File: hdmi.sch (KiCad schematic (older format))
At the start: 31 parts, among them J1901 Mini-HDMI, Q1901 NX3020NAKS, Q1902 NX3020NAKS, Q1903 NX3020NAKS, Q1904 NX3020NAKS, U1901 PCMF3HDMI2SZ, U1902 PCMF2HDMI2SZ

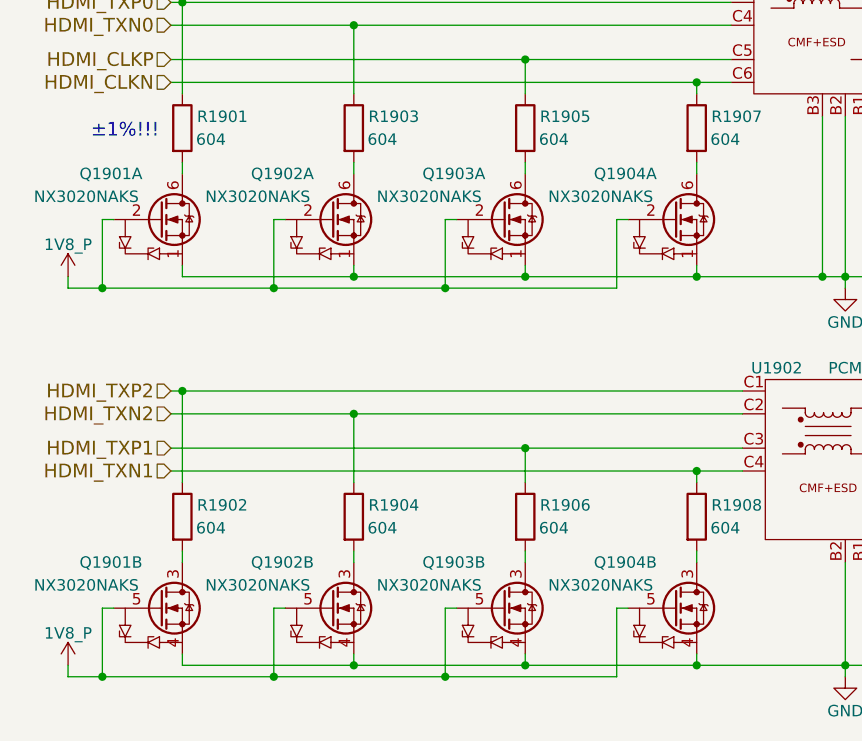
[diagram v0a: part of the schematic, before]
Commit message: Add preliminary Bill-of-Materials, fill in more missing component information such as inductor selection for the 3V3(_P) rail
Most critical components should now be getting ordered.
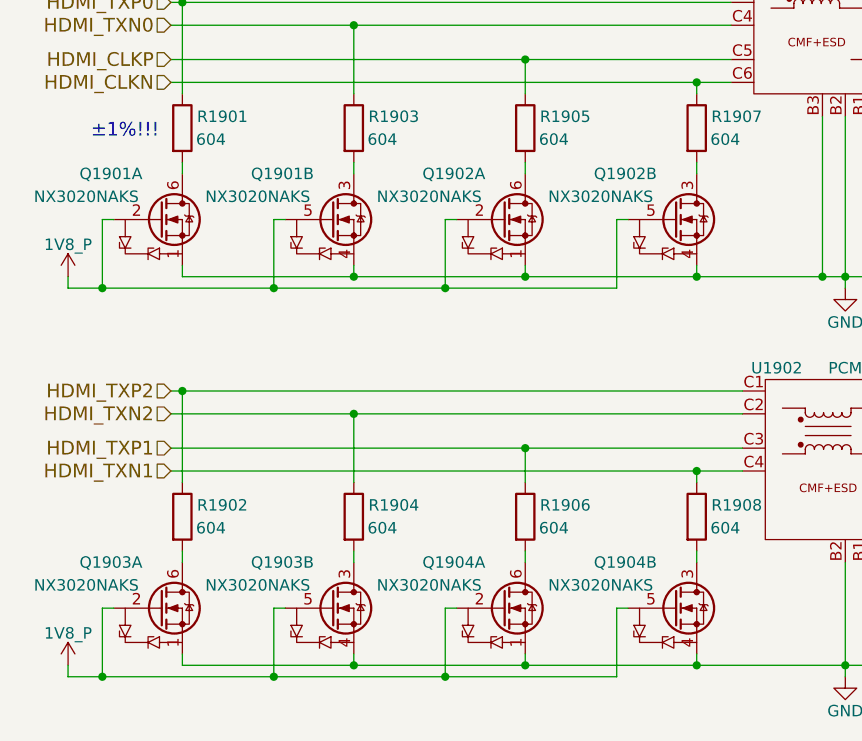
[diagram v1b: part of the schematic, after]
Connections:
- net at Q1902.6 (D): now also R1905.2; no longer R1903.2
- net at Q1903.6 (D): now also R1902.2; no longer R1905.2
- net at Q1904.6 (D): now also R1906.2; no longer R1907.2
- net at Q1901.3 (D): now also R1903.2; no longer R1902.2
- net at Q1902.3 (D): now also R1907.2; no longer R1904.2
- net at Q1903.3 (D): now also R1904.2; no longer R1906.2
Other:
- moved on the sheet: Q1901B, Q1902A, Q1902B, Q1903A, Q1903B, Q1904A
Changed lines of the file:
@@
 L Q_NMOS_DUAL Q1902
 U 1 1 5B013E98
-P 1800 3100
-F 0 "Q1902" H 1450 3300 50  0000 L CNN
-F 1 "NX3020NAKS" H 1250 3200 50  0000 L CNN
-F 2 "" H 2000 3200 50  0001 C CNN
-F 3 "" H 1800 3100 50  0001 C CNN
-	1    1800 3100
+P 2550 3100
+F 0 "Q1902" H 2200 3300 50  0000 L CNN
+F 1 "NX3020NAKS" H 2000 3200 50  0000 L CNN
+F 2 "" H 2750 3200 50  0001 C CNN
+F 3 "" H 2550 3100 50  0001 C CNN
+	1    2550 3100
 	1    0    0    -1
 $EndComp
@@
 L Q_NMOS_DUAL Q1903
 U 1 1 5B014489
-P 2550 3100
-F 0 "Q1903" H 2200 3300 50  0000 L CNN
-F 1 "NX3020NAKS" H 2000 3200 50  0000 L CNN
-F 2 "" H 2750 3200 50  0001 C CNN
-F 3 "" H 2550 3100 50  0001 C CNN
-	1    2550 3100
+P 1050 4800
+F 0 "Q1903" H 700 5000 50  0000 L CNN
+F 1 "NX3020NAKS" H 500 4900 50  0000 L CNN
+F 2 "" H 1250 4900 50  0001 C CNN
+F 3 "" H 1050 4800 50  0001 C CNN
+	1    1050 4800
 	1    0    0    -1
 $EndComp
@@
 L Q_NMOS_DUAL Q1904
 U 1 1 5B014490
-P 3300 3100
-F 0 "Q1904" H 2950 3300 50  0000 L CNN
-F 1 "NX3020NAKS" H 2750 3200 50  0000 L CNN
-F 2 "" H 3500 3200 50  0001 C CNN
-F 3 "" H 3300 3100 50  0001 C CNN
-	1    3300 3100
+P 2550 4800
+F 0 "Q1904" H 2200 5000 50  0000 L CNN
+F 1 "NX3020NAKS" H 2000 4900 50  0000 L CNN
+F 2 "" H 2750 4900 50  0001 C CNN
+F 3 "" H 2550 4800 50  0001 C CNN
+	1    2550 4800
 	1    0    0    -1
 $EndComp
@@
 L Q_NMOS_DUAL Q1901
 U 2 1 5B019D36
-P 1050 4800
-F 0 "Q1901" H 700 5000 50  0000 L CNN
-F 1 "NX3020NAKS" H 500 4900 50  0000 L CNN
-F 2 "" H 1250 4900 50  0001 C CNN
-F 3 "" H 1050 4800 50  0001 C CNN
-	2    1050 4800
+P 1800 3100
+F 0 "Q1901" H 1450 3300 50  0000 L CNN
+F 1 "NX3020NAKS" H 1250 3200 50  0000 L CNN
+F 2 "" H 2000 3200 50  0001 C CNN
+F 3 "" H 1800 3100 50  0001 C CNN
+	2    1800 3100
 	1    0    0    -1
 $EndComp
@@
 L Q_NMOS_DUAL Q1902
 U 2 1 5B019D3C
-P 1800 4800
-F 0 "Q1902" H 1450 5000 50  0000 L CNN
-F 1 "NX3020NAKS" H 1250 4900 50  0000 L CNN
-F 2 "" H 2000 4900 50  0001 C CNN
-F 3 "" H 1800 4800 50  0001 C CNN
-	2    1800 4800
+P 3300 3100
+F 0 "Q1902" H 2950 3300 50  0000 L CNN
+F 1 "NX3020NAKS" H 2750 3200 50  0000 L CNN
+F 2 "" H 3500 3200 50  0001 C CNN
+F 3 "" H 3300 3100 50  0001 C CNN
+	2    3300 3100
 	1    0    0    -1
 $EndComp
@@
 L Q_NMOS_DUAL Q1903
 U 2 1 5B019D4E
-P 2550 4800
-F 0 "Q1903" H 2200 5000 50  0000 L CNN
-F 1 "NX3020NAKS" H 2000 4900 50  0000 L CNN
-F 2 "" H 2750 4900 50  0001 C CNN
-F 3 "" H 2550 4800 50  0001 C CNN
-	2    2550 4800
+P 1800 4800
+F 0 "Q1903" H 1450 5000 50  0000 L CNN
+F 1 "NX3020NAKS" H 1250 4900 50  0000 L CNN
+F 2 "" H 2000 4900 50  0001 C CNN
+F 3 "" H 1800 4800 50  0001 C CNN
+	2    1800 4800
 	1    0    0    -1
 $EndComp

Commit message: Add decoupling/stitching capacitors to the 5V_P, 3V3_P, and 1V8_P rails which will be spread through the respective power planes (not necessarily having to be near chips)
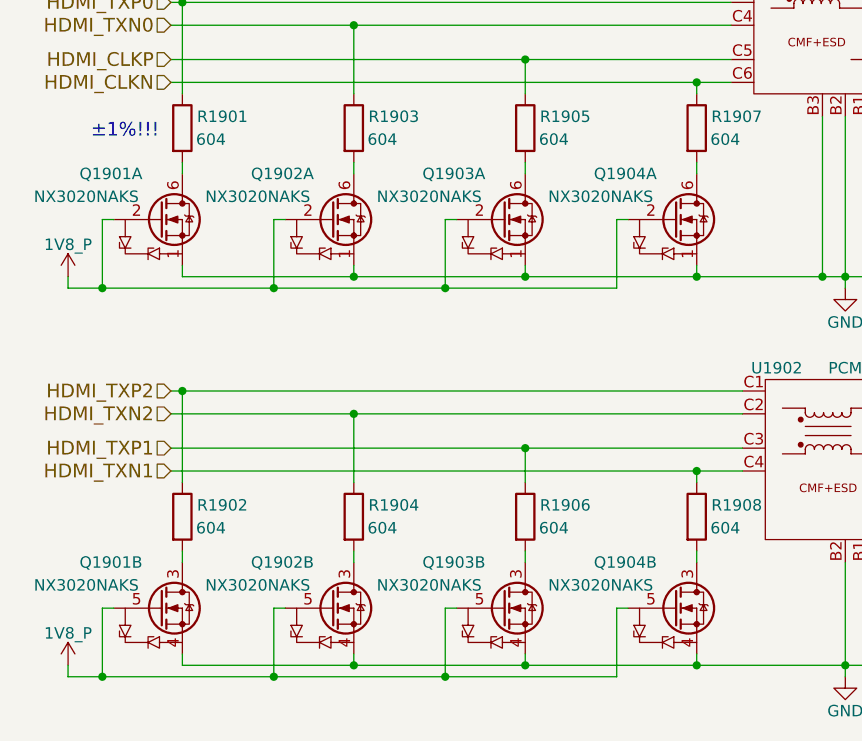
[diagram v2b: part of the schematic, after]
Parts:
- renumbered Q1903 to Q1901, Q1901 to Q1902, Q1903 to Q1902, Q1902 to Q1903, Q1904 to Q1903, Q1902 to Q1904
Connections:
- net 1V8_P: now also Q1901.5 (G), Q1902.2 (G), Q1903.5 (G), Q1904.2 (G); no longer Q1901.2 (G), Q1902.5 (G), Q1903.2 (G), Q1904.5 (G)
- net GND: now also Q1901.4 (S), Q1902.1 (S), Q1903.4 (S), Q1904.1 (S); no longer Q1901.1 (S), Q1902.4 (S), Q1903.1 (S), Q1904.4 (S)
- net at R1903.2: now also Q1902.6 (D); no longer Q1902.3 (D)
- net at R1902.2: now also Q1901.3 (D); no longer Q1901.6 (D)
- net at R1906.2: now also Q1903.3 (D); no longer Q1903.6 (D)
- net at R1907.2: now also Q1904.6 (D); no longer Q1904.3 (D)
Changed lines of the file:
@@
 Sheet 19 24
 Title "HDMI"
-Date "2018-06-01"
+Date "2018-06-06"
 Rev "v0.1.0"
 Comp "Purism SPC"
@@
 $EndComp
 $Comp
-L Q_NMOS_DUAL Q1902
+L Q_NMOS_DUAL Q1903
 U 1 1 5B013E98
 P 2550 3100
-F 0 "Q1902" H 2200 3300 50  0000 L CNN
+F 0 "Q1903" H 2200 3300 50  0000 L CNN
 F 1 "NX3020NAKS" H 2000 3200 50  0000 L CNN
 F 2 "" H 2750 3200 50  0001 C CNN
@@
 $EndComp
 $Comp
-L Q_NMOS_DUAL Q1903
-U 1 1 5B014489
+L Q_NMOS_DUAL Q1901
+U 2 1 5B014489
 P 1050 4800
-F 0 "Q1903" H 700 5000 50  0000 L CNN
+F 0 "Q1901" H 700 5000 50  0000 L CNN
 F 1 "NX3020NAKS" H 500 4900 50  0000 L CNN
 F 2 "" H 1250 4900 50  0001 C CNN
 F 3 "" H 1050 4800 50  0001 C CNN
-	1    1050 4800
-	1    0    0    -1
-$EndComp
-$Comp
-L Q_NMOS_DUAL Q1904
-U 1 1 5B014490
+	2    1050 4800
+	1    0    0    -1
+$EndComp
+$Comp
+L Q_NMOS_DUAL Q1903
+U 2 1 5B014490
 P 2550 4800
-F 0 "Q1904" H 2200 5000 50  0000 L CNN
+F 0 "Q1903" H 2200 5000 50  0000 L CNN
 F 1 "NX3020NAKS" H 2000 4900 50  0000 L CNN
 F 2 "" H 2750 4900 50  0001 C CNN
 F 3 "" H 2550 4800 50  0001 C CNN
-	1    2550 4800
+	2    2550 4800
 	1    0    0    -1
 $EndComp
@@
 $EndComp
 $Comp
-L 1V8_P #PWR0334
+L 1V8_P #PWR0340
 U 1 1 5B01672B
 P 650 3350
-F 0 "#PWR0334" H 650 3200 50  0001 C CNN
+F 0 "#PWR0340" H 650 3200 50  0001 C CNN
 F 1 "1V8_P" H 650 3490 50  0000 C CNN
 F 2 "" H 650 3350 50  0001 C CNN
@@
 $EndComp
 $Comp
-L Q_NMOS_DUAL Q1901
-U 2 1 5B019D36
+L Q_NMOS_DUAL Q1902
+U 1 1 5B019D36
 P 1800 3100
-F 0 "Q1901" H 1450 3300 50  0000 L CNN
+F 0 "Q1902" H 1450 3300 50  0000 L CNN
 F 1 "NX3020NAKS" H 1250 3200 50  0000 L CNN
 F 2 "" H 2000 3200 50  0001 C CNN
 F 3 "" H 1800 3100 50  0001 C CNN
-	2    1800 3100
-	1    0    0    -1
-$EndComp
-$Comp
-L Q_NMOS_DUAL Q1902
-U 2 1 5B019D3C
+	1    1800 3100
+	1    0    0    -1
+$EndComp
+$Comp
+L Q_NMOS_DUAL Q1904
+U 1 1 5B019D3C
 P 3300 3100
-F 0 "Q1902" H 2950 3300 50  0000 L CNN
+F 0 "Q1904" H 2950 3300 50  0000 L CNN
 F 1 "NX3020NAKS" H 2750 3200 50  0000 L CNN
 F 2 "" H 3500 3200 50  0001 C CNN
 F 3 "" H 3300 3100 50  0001 C CNN
-	2    3300 3100
+	1    3300 3100
 	1    0    0    -1
 $EndComp
@@
 $EndComp
 $Comp
-L Q_NMOS_DUAL Q1903
+L Q_NMOS_DUAL Q1902
 U 2 1 5B019D4E
 P 1800 4800
-F 0 "Q1903" H 1450 5000 50  0000 L CNN
+F 0 "Q1902" H 1450 5000 50  0000 L CNN
 F 1 "NX3020NAKS" H 1250 4900 50  0000 L CNN
 F 2 "" H 2000 4900 50  0001 C CNN
@@
 $EndComp
 $Comp
-L 1V8_P #PWR0335
+L 1V8_P #PWR0341
 U 1 1 5B019D66
 P 650 5050
-F 0 "#PWR0335" H 650 4900 50  0001 C CNN
+F 0 "#PWR0341" H 650 4900 50  0001 C CNN
 F 1 "1V8_P" H 650 5190 50  0000 C CNN
 F 2 "" H 650 5050 50  0001 C CNN
@@
 ±1%!!!
 $Comp
-L GND #PWR0336
+L GND #PWR0342
 U 1 1 5B081BE1
 P 4050 3400
-F 0 "#PWR0336" H 4050 3150 50  0001 C CNN
+F 0 "#PWR0342" H 4050 3150 50  0001 C CNN
 F 1 "GND" H 4050 3250 50  0000 C CNN
 F 2 "" H 4050 3400 50  0001 C CNN
@@
 HDMI_TXN1
 $Comp
-L GND #PWR0337
+L GND #PWR0343
 U 1 1 5B08911B
 P 4050 5100
-F 0 "#PWR0337" H 4050 4850 50  0001 C CNN
+F 0 "#PWR0343" H 4050 4850 50  0001 C CNN
 F 1 "GND" H 4050 4950 50  0000 C CNN
 F 2 "" H 4050 5100 50  0001 C CNN
@@
 $EndComp
 $Comp
-L GND #PWR0338
+L GND #PWR0344
 U 1 1 5AF69B9C
 P 9100 4900
-F 0 "#PWR0338" H 9100 4650 50  0001 C CNN
+F 0 "#PWR0344" H 9100 4650 50  0001 C CNN
 F 1 "GND" H 9100 4750 50  0000 C CNN
 F 2 "" H 9100 4900 50  0001 C CNN
@@
 $EndComp
 $Comp
-L GND #PWR0339
+L GND #PWR0345
 U 1 1 5AFABCE1
 P 5900 2400
-F 0 "#PWR0339" H 5900 2150 50  0001 C CNN
+F 0 "#PWR0345" H 5900 2150 50  0001 C CNN
 F 1 "GND" H 5900 2250 50  0000 C CNN
 F 2 "" H 5900 2400 50  0001 C CNN
@@
 	9100 2350 9100 4500
 $Comp
-L 3V3_P #PWR0340
+L 3V3_P #PWR0346
 U 1 1 5AFBD440
 P 9100 1650
-F 0 "#PWR0340" H 9100 1500 50  0001 C CNN
+F 0 "#PWR0346" H 9100 1500 50  0001 C CNN
 F 1 "3V3_P" H 9100 1790 50  0000 C CNN
 F 2 "" H 9100 1650 50  0001 C CNN
@@
 Connection ~ 10450 2150
 $Comp
-L 5V_P #PWR0341
+L 5V_P #PWR0347
 U 1 1 5B3E4E0C
 P 5800 1800
-F 0 "#PWR0341" H 5800 1650 50  0001 C CNN
+F 0 "#PWR0347" H 5800 1650 50  0001 C CNN
 F 1 "5V_P" H 5800 1940 50  0000 C CNN
 F 2 "" H 5800 1800 50  0001 C CNN

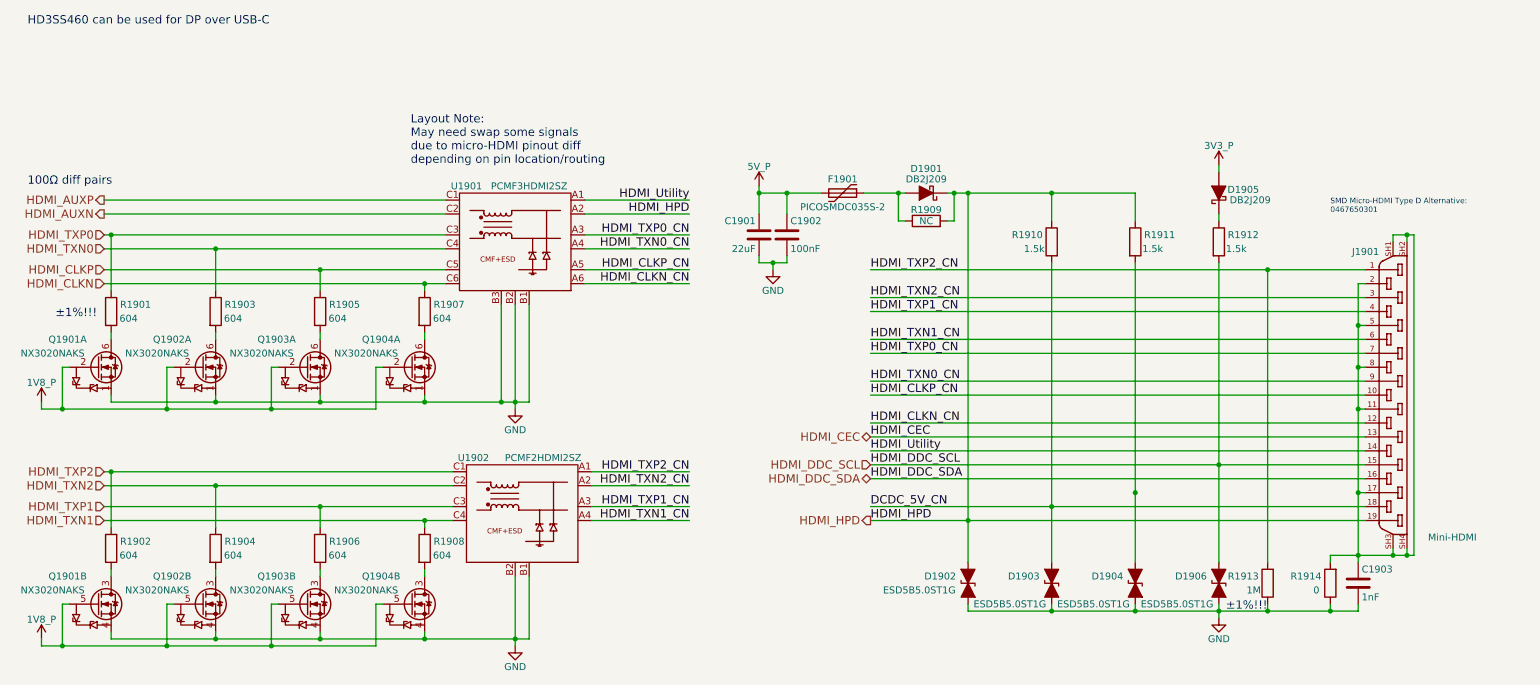
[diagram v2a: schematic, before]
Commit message: Assign footprints and component properties to all diodes (including LEDs)
Using Lite-On's LTST-C190GKT (0603, 2.1V @ 20mA) instead of Broadcom's HSMG-C170 (0805, 2.2V @ 20mA) in the ethernet circuit.
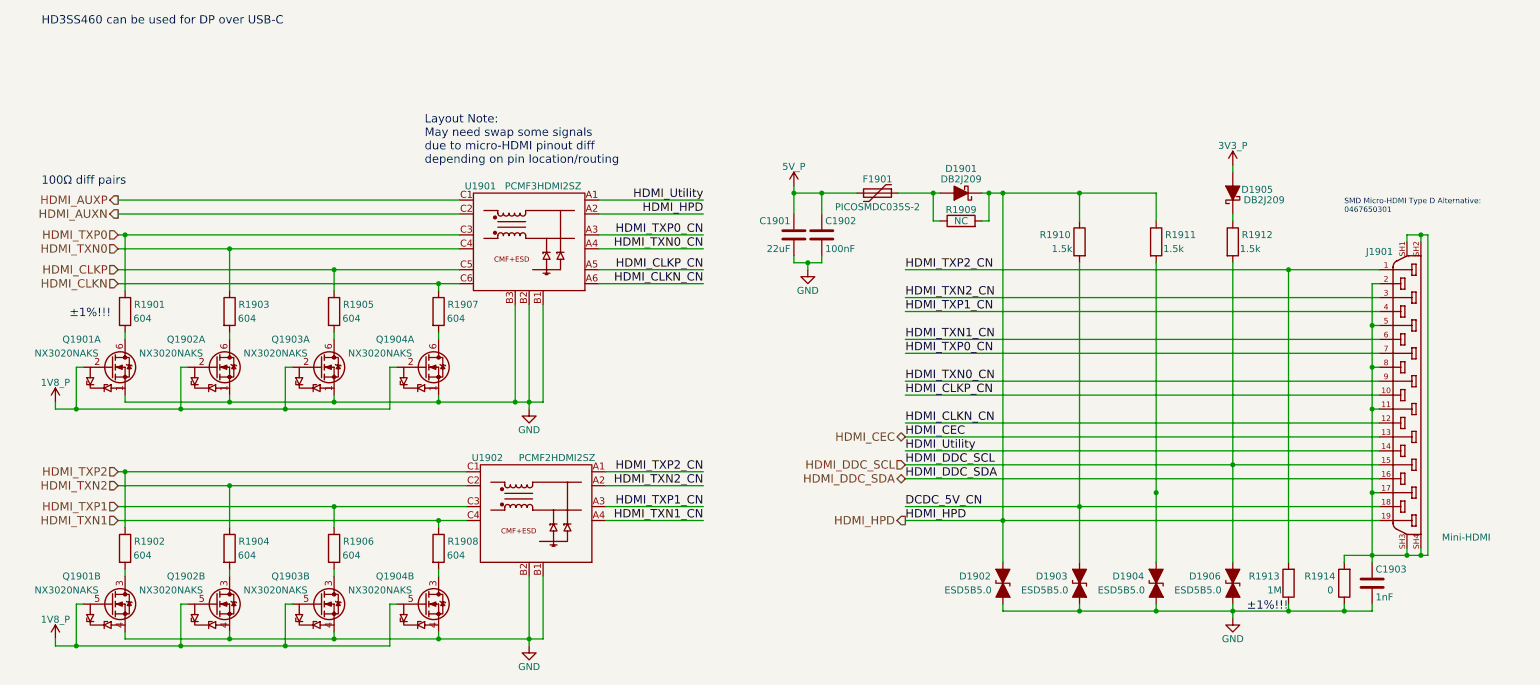
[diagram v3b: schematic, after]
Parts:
- D1901, D1905: footprint (none) -> dvk-mx8m-bsb:SMini2-F5-B
- D1902, D1903, D1904, D1906: value ESD5B5.0ST1G -> ESD5B5.0; footprint (none) -> dvk-mx8m-bsb:SOD-523_Case-502; Distrib Link (none) -> http://www.newark.com/on-semiconductor/esd5b5-0st1g/tvs-dio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; Distrib PN (none) -> ESD5B5.0ST1GOSCT-ND; MFG Name (none) -> ON Semiconductor; MFG Part Num (none) -> ESD5B5.0ST1G; Others (none) -> https://octopart.com/search?q=ESD5B5.0ST1G&start=0; Tolerance (none) -> -
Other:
- moved on the sheet: C1901, C1902, C1903, D1901, D1905, F1901, J1901, Q1901A, Q1901B, Q1902A, Q1902B, Q1903A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

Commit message: Add polyfuse/PTC resettable fuse footprints and 3D models
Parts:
- F1901: footprint (none) -> dvk-mx8m-bsb:Fuse_SMD0805_Reflow
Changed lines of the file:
@@
 F 0 "F1901" V 6550 1850 50  0000 C CNN
 F 1 "PICOSMDC035S-2" V 6750 1850 50  0000 C CNN
-F 2 "" H 6700 1650 50  0001 L CNN
+F 2 "dvk-mx8m-bsb:Fuse_SMD0805_Reflow" H 6700 1650 50  0001 L CNN
 F 3 "" H 6650 1850 50  0001 C CNN
 	1    6650 1850
